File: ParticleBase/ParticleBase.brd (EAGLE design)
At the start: 109.2 x 61 mm, 34 parts

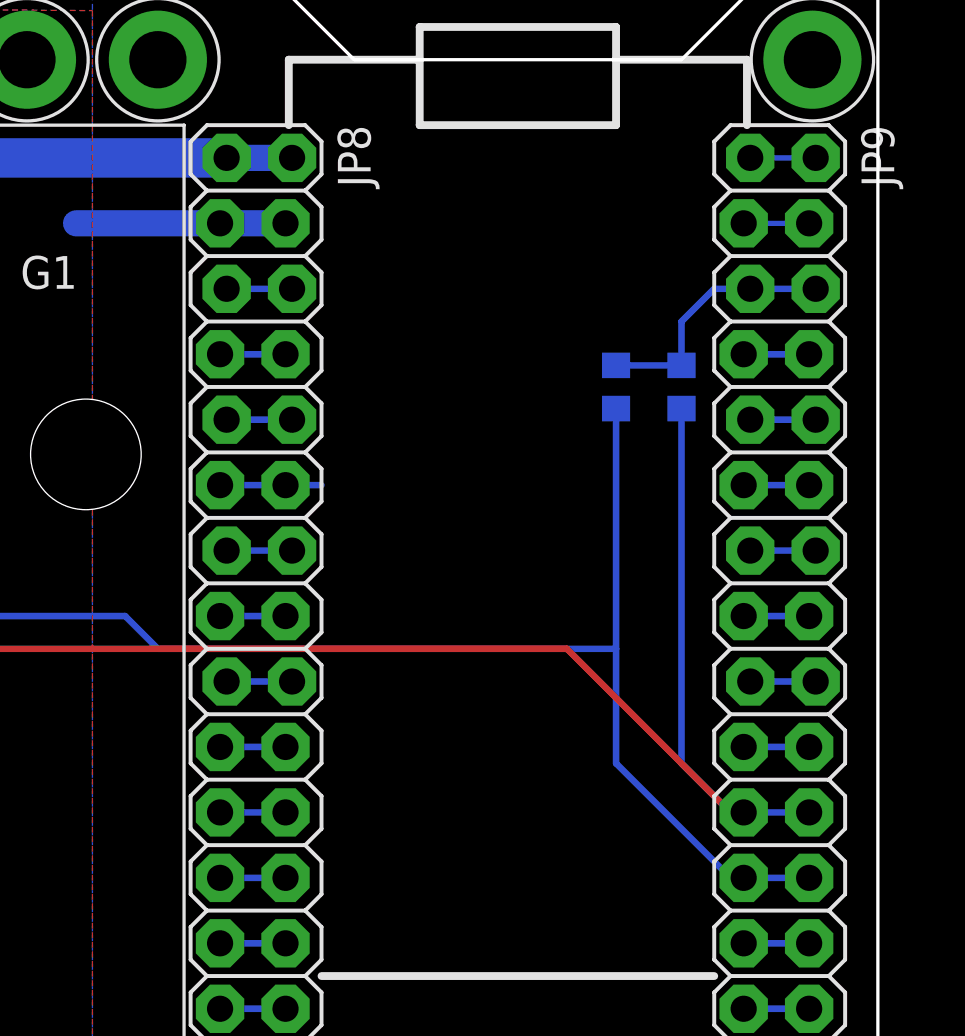
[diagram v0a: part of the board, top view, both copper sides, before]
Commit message: Fixed 3.3V connection. The old pin worked with the Spark but not the Photon.
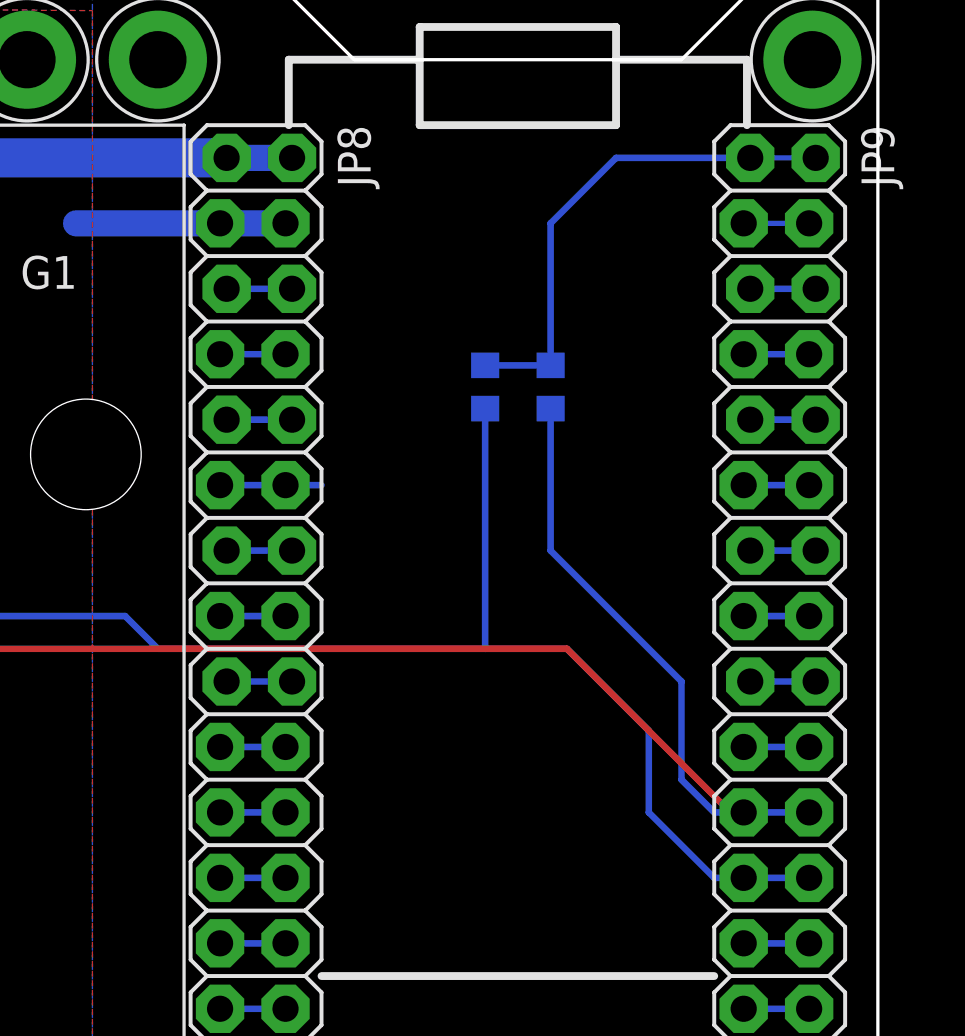
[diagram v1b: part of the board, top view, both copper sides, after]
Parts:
- moved R1 5.08 mm to (96.5, 45.7)
- moved R2 5.08 mm to (94.0, 45.7)
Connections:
- removed net N$19: JP9.1, JP9.2
- new net N$14: JP9.5, JP9.6
- net 3.3V: now also JP9.1, JP9.2; no longer JP9.5, JP9.6
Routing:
- net 3.3V: track 9.97 -> 19.4 mm
- net N$19: track 2.54 -> 0.00 mm
- net N$14: track 0.00 -> 2.54 mm
- net SCL: track 188.3 -> 190.7 mm
- net SDA: track 167.7 -> 167.0 mm
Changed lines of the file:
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@@
 <attribute name="PARTNUM" value="EXCLUDE" x="81.28" y="2.54" size="1.778" layer="27" display="off"/>
 </element>
-<element name="R2" library="Modulo" package="0603" value="1KΩ" x="99.06" y="45.72" rot="MR270">
-<attribute name="PARTNUM" value="ERJ-3EKF1001V" x="78.74" y="58.42" size="1.778" layer="28" rot="MR270" display="off"/>
-</element>
-<element name="R1" library="Modulo" package="0603" value="1KΩ" x="101.6" y="45.72" rot="MR270">
-<attribute name="PARTNUM" value="ERJ-3EKF1001V" x="85.09" y="54.61" size="1.778" layer="28" rot="MR270" display="off"/>
+<element name="R2" library="Modulo" package="0603" value="1KΩ" x="93.98" y="45.72" rot="MR270">
+<attribute name="PARTNUM" value="ERJ-3EKF1001V" x="73.66" y="58.42" size="1.778" layer="28" rot="MR270" display="off"/>
+</element>
+<element name="R1" library="Modulo" package="0603" value="1KΩ" x="96.52" y="45.72" rot="MR270">
+<attribute name="PARTNUM" value="ERJ-3EKF1001V" x="80.01" y="54.61" size="1.778" layer="28" rot="MR270" display="off"/>
 </element>
 <element name="C1" library="Modulo" package="PANASONIC_D" value="56uF" x="68.58" y="48.26" rot="MR90">
@@
 <contactref element="JP9" pad="24"/>
 <contactref element="JP9" pad="23"/>
-<wire x1="104.013" y1="26.67" x2="103.505" y2="26.67" width="0.254" layer="16"/>
-<wire x1="103.505" y1="26.67" x2="99.06" y2="31.115" width="0.254" layer="16"/>
-<wire x1="99.06" y1="31.115" x2="99.06" y2="35.56" width="0.254" layer="16"/>
-<wire x1="99.06" y1="35.56" x2="99.06" y2="44.8818" width="0.254" layer="16"/>
 <wire x1="104.013" y1="26.67" x2="106.553" y2="26.67" width="0.254" layer="16"/>
-<wire x1="99.06" y1="35.56" x2="81.28" y2="35.56" width="0.254" layer="16"/>
 <wire x1="81.28" y1="35.56" x2="80.01" y2="36.83" width="0.254" layer="16"/>
 <wire x1="80.01" y1="36.83" x2="68.58" y2="36.83" width="0.254" layer="16"/>
@@
 <wire x1="58.928" y1="31.623" x2="59.182" y2="31.623" width="0.254" layer="16"/>
 <wire x1="59.182" y1="31.623" x2="61.468" y2="29.337" width="0.254" layer="16"/>
+<wire x1="104.013" y1="26.67" x2="102.87" y2="26.67" width="0.254" layer="16"/>
+<wire x1="102.87" y1="26.67" x2="100.33" y2="29.21" width="0.254" layer="16"/>
+<wire x1="100.33" y1="29.21" x2="100.33" y2="32.385" width="0.254" layer="16"/>
+<wire x1="100.33" y1="32.385" x2="97.155" y2="35.56" width="0.254" layer="16"/>
+<wire x1="97.155" y1="35.56" x2="93.98" y2="35.56" width="0.254" layer="16"/>
+<wire x1="93.98" y1="35.56" x2="93.98" y2="44.8818" width="0.254" layer="16"/>
+<wire x1="81.28" y1="35.56" x2="93.98" y2="35.56" width="0.254" layer="16"/>
 </signal>
 <signal name="SCL">
@@
 <contactref element="JP9" pad="22"/>
 <contactref element="JP9" pad="21"/>
-<wire x1="104.013" y1="29.21" x2="103.505" y2="29.21" width="0.254" layer="16"/>
-<wire x1="103.505" y1="29.21" x2="101.6" y2="31.115" width="0.254" layer="16"/>
-<wire x1="101.6" y1="31.115" x2="101.6" y2="44.8818" width="0.254" layer="16"/>
 <via x="66.04" y="35.56" extent="1-16" drill="0.4064"/>
 <wire x1="66.04" y1="35.56" x2="97.155" y2="35.56" width="0.254" layer="1"/>
@@
 <wire x1="64.643" y1="31.623" x2="66.04" y2="33.02" width="0.254" layer="16"/>
 <wire x1="66.04" y1="33.02" x2="66.04" y2="35.56" width="0.254" layer="16"/>
+<wire x1="104.013" y1="29.21" x2="102.87" y2="29.21" width="0.254" layer="16"/>
+<wire x1="102.87" y1="29.21" x2="101.6" y2="30.48" width="0.254" layer="16"/>
+<wire x1="101.6" y1="30.48" x2="101.6" y2="34.29" width="0.254" layer="16"/>
+<wire x1="101.6" y1="34.29" x2="96.52" y2="39.37" width="0.254" layer="16"/>
+<wire x1="96.52" y1="39.37" x2="96.52" y2="44.8818" width="0.254" layer="16"/>
 </signal>
 <signal name="GND">
@@
 <contactref element="R2" pad="1"/>
 <contactref element="R1" pad="1"/>
-<contactref element="JP9" pad="6"/>
-<contactref element="JP9" pad="5"/>
-<wire x1="99.06" y1="46.5582" x2="101.6" y2="46.5582" width="0.254" layer="16"/>
-<wire x1="104.267" y1="49.53" x2="102.87" y2="49.53" width="0.254" layer="16"/>
-<wire x1="102.87" y1="49.53" x2="101.6" y2="48.26" width="0.254" layer="16"/>
-<wire x1="101.6" y1="48.26" x2="101.6" y2="46.5582" width="0.254" layer="16"/>
-<wire x1="106.807" y1="49.53" x2="104.267" y2="49.53" width="0.254" layer="16"/>
+<wire x1="93.98" y1="46.5582" x2="96.52" y2="46.5582" width="0.254" layer="16"/>
+<contactref element="JP9" pad="1"/>
+<contactref element="JP9" pad="2"/>
+<wire x1="106.807" y1="54.61" x2="104.267" y2="54.61" width="0.2032" layer="16"/>
+<wire x1="96.52" y1="46.5582" x2="96.52" y2="52.07" width="0.254" layer="16"/>
+<wire x1="96.52" y1="52.07" x2="99.06" y2="54.61" width="0.254" layer="16"/>
+<wire x1="99.06" y1="54.61" x2="104.267" y2="54.61" width="0.254" layer="16"/>
 </signal>
 <signal name="N$1">
@@
 <wire x1="83.693" y1="11.43" x2="86.233" y2="11.43" width="0.254" layer="16"/>
 </signal>
-<signal name="N$19">
-<contactref element="JP9" pad="1"/>
-<contactref element="JP9" pad="2"/>
-<wire x1="106.807" y1="54.61" x2="104.267" y2="54.61" width="0.2032" layer="16"/>
-</signal>
 <signal name="N$20">
 <contactref element="JP9" pad="4"/>
@@
 <wire x1="106.553" y1="11.43" x2="104.013" y2="11.43" width="0.254" layer="16"/>
 </signal>
+<signal name="N$14">
+<contactref element="JP9" pad="5"/>
+<contactref element="JP9" pad="6"/>
+<wire x1="104.267" y1="49.53" x2="106.807" y2="49.53" width="0.254" layer="16"/>
+</signal>
 </signals>

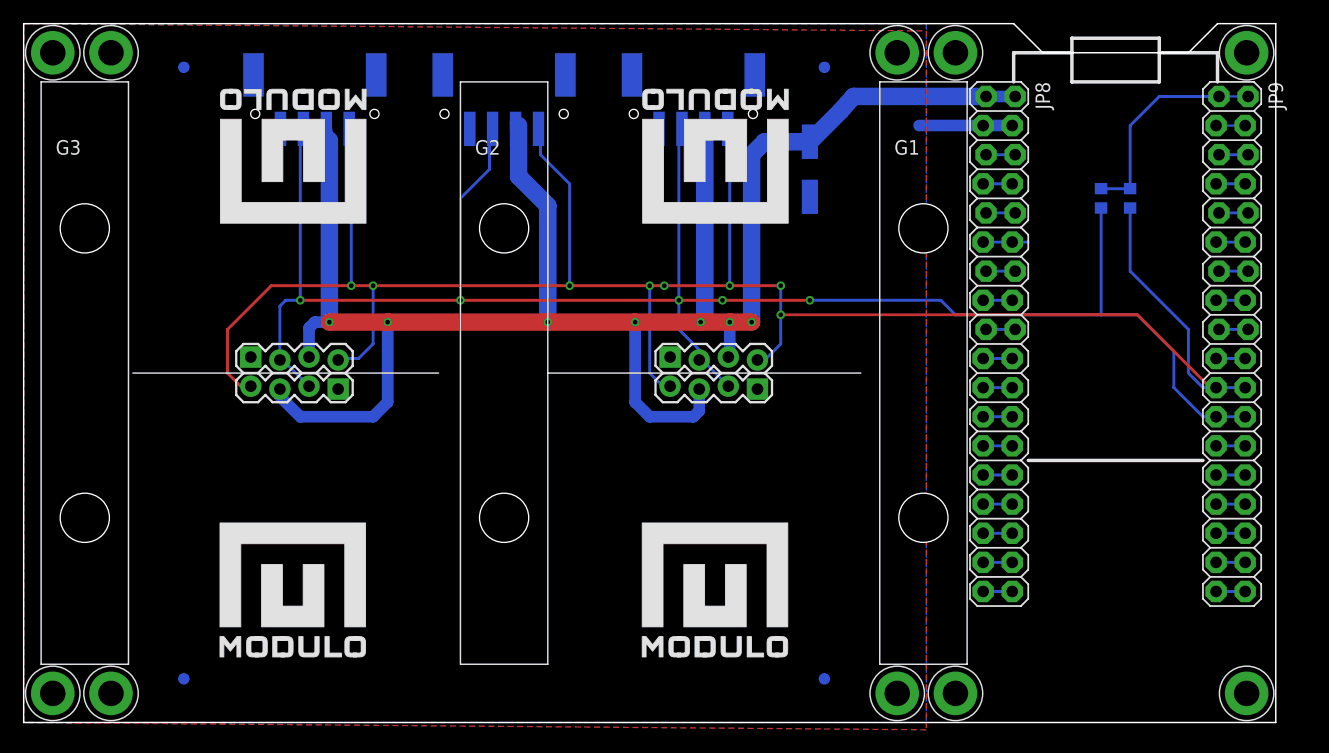
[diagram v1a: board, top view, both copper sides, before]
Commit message: New Grove compatible connector footprint
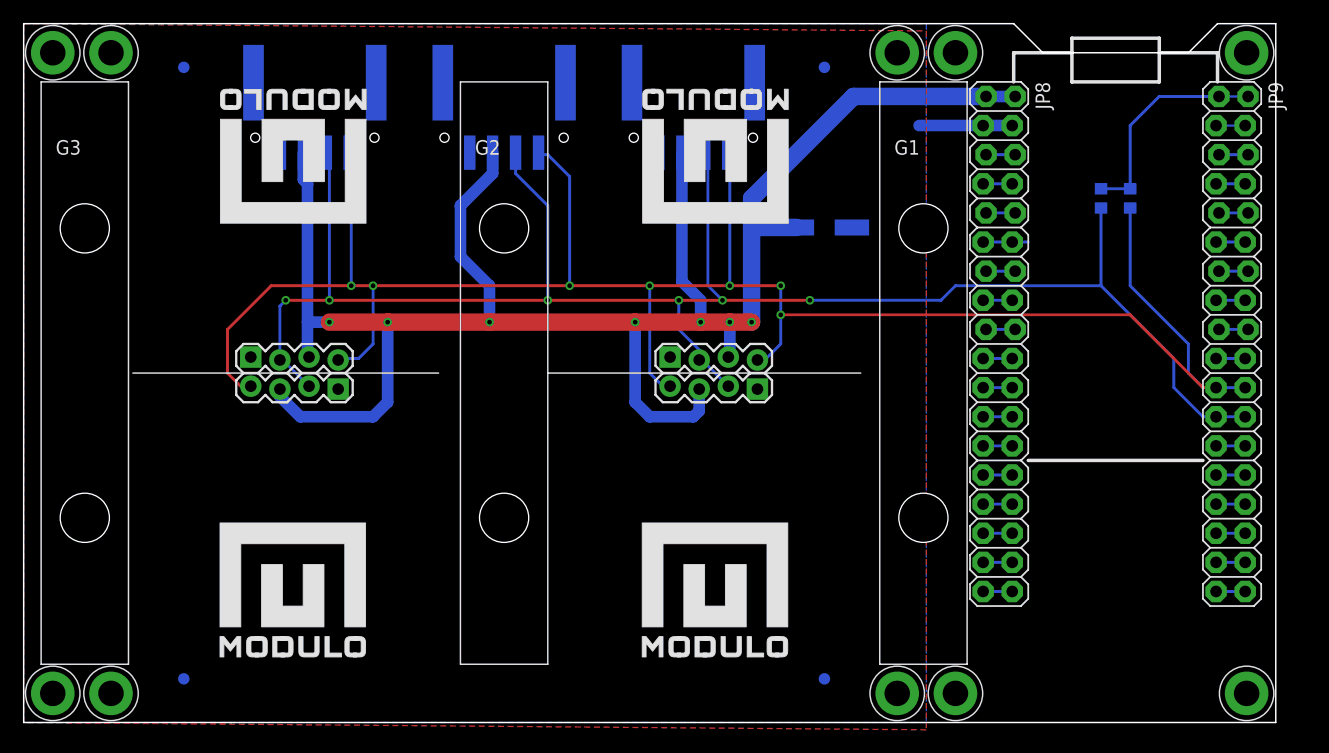
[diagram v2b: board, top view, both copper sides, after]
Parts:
- JP2, JP4, JP7: value HEADER-1X4-JST-PA-SIDE-SMD -> HEADER-MODULO
- moved JP4 33.0 mm to (58.4, 61.0)
- moved JP7 33.0 mm to (25.4, 61.0)
- moved C1 5.24 mm to (69.8, 43.2), turned to 0 degrees
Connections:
- net SDA: now also JP2.3, JP4.3, JP7.3; no longer JP2.2, JP4.2, JP7.2
- net VCC: now also JP2.2, JP4.2, JP7.2; no longer JP2.3, JP4.3, JP7.3
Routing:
- net SDA: track 167.0 -> 156.4 mm, vias 5 -> 6
- net SCL: track 190.7 -> 181.8 mm, vias 8 -> 7
- net VCC: track 170.7 -> 167.2 mm

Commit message: Various updates
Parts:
- added D1, D2: RB751V40, Modulo:SOD-323
- added U$6: (no value), WorksWithParticle:WORKS_WITH_PARTICLE_LOGO_LARGE
- moved F3 33.7 mm to (103.5, 3.81)
- moved F4 29.8 mm to (99.7, 57.1)
- moved H10 2.54 mm to (109.2, 58.4)
- moved H5 2.54 mm to (109.2, 2.54)
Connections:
- net 3.3V: now also D1.C, D2.C
- net SCL: now also D1.A
- net SDA: now also D2.A
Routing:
- net 3.3V: track 19.4 -> 27.3 mm
- net SDA: track 156.4 -> 160.3 mm
- net SCL: track 181.8 -> 185.7 mm
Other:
- board size 109.2 x 61 mm -> 111.8 x 61 mm

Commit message: Various small tweaks based on testing and feedback from manufacturer.
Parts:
- added C2: 10uF, Modulo:0603
- added R3, R4: 12Ω, Modulo:0603
- added U1: VREG-MIC5205-3.3V, Modulo:SOT23-5
- R1, R2: value 1KΩ -> 5kΩ
- moved D1 3.81 mm to (100.3, 41.9)
- moved D2 3.81 mm to (90.2, 41.9)
- moved R1 3.81 mm to (96.5, 41.9)
- moved R2 3.81 mm to (94.0, 41.9)
- moved F4 2.84 mm to (97.2, 55.9)
- moved F1 2.54 mm to (14.0, 6.35)
- moved F2 2.54 mm to (14.0, 54.6)
- moved F3 1.80 mm to (102.2, 5.08)
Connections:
- new net N$16: D1.C, R3.2
- new net N$19: D2.C, R4.2
- new net N$34: JP9.1, JP9.2
- net 3.3V: now also C2.2, R3.1, R4.1, U1.5; no longer D1.C, D2.C, JP9.1, JP9.2
- net GND: now also C2.1, U1.2
- net VCC: now also U1.1, U1.3
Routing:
- net VCC: track 167.2 -> 190.1 mm
- net GND: track 8.13 -> 22.8 mm
- net 3.3V: track 27.3 -> 19.1 mm
- net N$19: track 0.00 -> 2.74 mm
- net N$16: track 0.00 -> 2.74 mm
- net N$34: track 0.00 -> 2.54 mm

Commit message: Various minor tweaks based on testing and feedback from manufacturer
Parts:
- added SJ1: SOLDERJUMPERNO, SparkFun-Passives:SJ_2S-NO
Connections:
- net 3.3V: now also SJ1.2
- net N$34: now also SJ1.1
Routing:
- net N$34: track 2.54 -> 9.88 mm
- net 3.3V: track 19.1 -> 23.5 mm
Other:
- board text added: "v1"
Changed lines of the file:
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@@
 <wire x1="89.535" y1="22.86" x2="86.995" y2="25.4" width="0.254" layer="21"/>
 <wire x1="91.44" y1="58.42" x2="99.06" y2="58.42" width="0.254" layer="21"/>
+<text x="110.49" y="6.35" size="1.524" layer="22" rot="MR0">v1</text>
 </plain>
 <attributes>
@@
 <attribute name="PARTNUM" value="GRM188R61C106MA73D" x="90.17" y="49.53" size="1.778" layer="28" rot="MR270" display="off"/>
 </element>
+<element name="SJ1" library="SparkFun-Passives" package="SJ_2S-NO" value="SOLDERJUMPERNO" x="100.33" y="49.53" smashed="yes" rot="MR0">
+<attribute name="NAME" x="98.698" y="49.53" size="0.4064" layer="26" rot="MR0"/>
+</element>
 </elements>
 <signals>
@@
 <wire x1="91.44" y1="48.895" x2="90.3732" y2="48.895" width="0.254" layer="16"/>
 <wire x1="90.3732" y1="48.895" x2="90.17" y2="48.6918" width="0.254" layer="16"/>
+<contactref element="SJ1" pad="2"/>
+<wire x1="99.88" y1="49.53" x2="99.695" y2="49.53" width="0.254" layer="16"/>
+<wire x1="99.695" y1="49.53" x2="99.06" y2="48.895" width="0.254" layer="16"/>
+<wire x1="99.06" y1="48.895" x2="99.06" y2="45.9232" width="0.254" layer="16"/>
+<wire x1="99.06" y1="45.9232" x2="98.8568" y2="45.72" width="0.254" layer="16"/>
 </signal>
 <signal name="N$1">
@@
 <contactref element="JP9" pad="2"/>
 <wire x1="104.267" y1="54.61" x2="106.807" y2="54.61" width="0.254" layer="16"/>
+<contactref element="SJ1" pad="1"/>
+<wire x1="104.267" y1="54.61" x2="102.87" y2="54.61" width="0.254" layer="16"/>
+<wire x1="102.87" y1="54.61" x2="100.965" y2="52.705" width="0.254" layer="16"/>
+<wire x1="100.965" y1="52.705" x2="100.965" y2="49.715" width="0.254" layer="16"/>
+<wire x1="100.965" y1="49.715" x2="100.78" y2="49.53" width="0.254" layer="16"/>
 </signal>
 </signals>

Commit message: Added unique board prefixes to part numbers due to CM requirements
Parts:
- added 1-FOOT1, 1-FOOT2, 1-FOOT3, 1-FOOT4: FOOT, Modulo:FOOT
- renumbered C1 to 1-C1, C2 to 1-C2, D1 to 1-D1, D2 to 1-D2, G1 to 1-G1, G2 to 1-G2, G3 to 1-G3, JP1 to 1-JP1, JP2 to 1-JP2, JP3 to 1-JP3, JP4 to 1-JP4, JP5 to 1-JP5, JP6 to 1-JP6, JP7 to 1-JP7, JP8 to 1-JP8, JP9 to 1-JP9, R1 to 1-R1, R2 to 1-R2, R3 to 1-R3, R4 to 1-R4, SJ1 to 1-SJ1, U1 to 1-U1
